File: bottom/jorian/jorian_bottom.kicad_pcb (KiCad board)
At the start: 2 copper layers, 152.4 x 85.1 mm, 7 parts

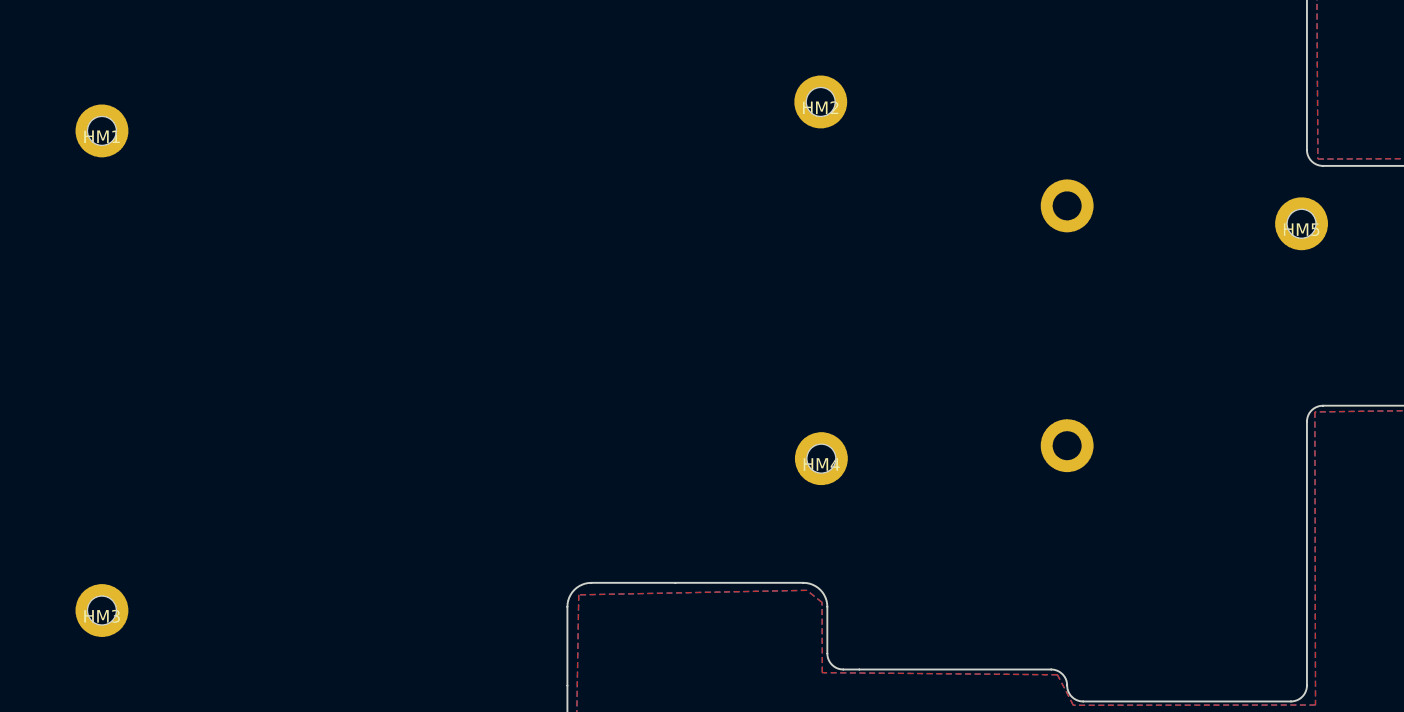
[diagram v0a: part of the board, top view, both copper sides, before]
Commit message: Updated case hole footprints
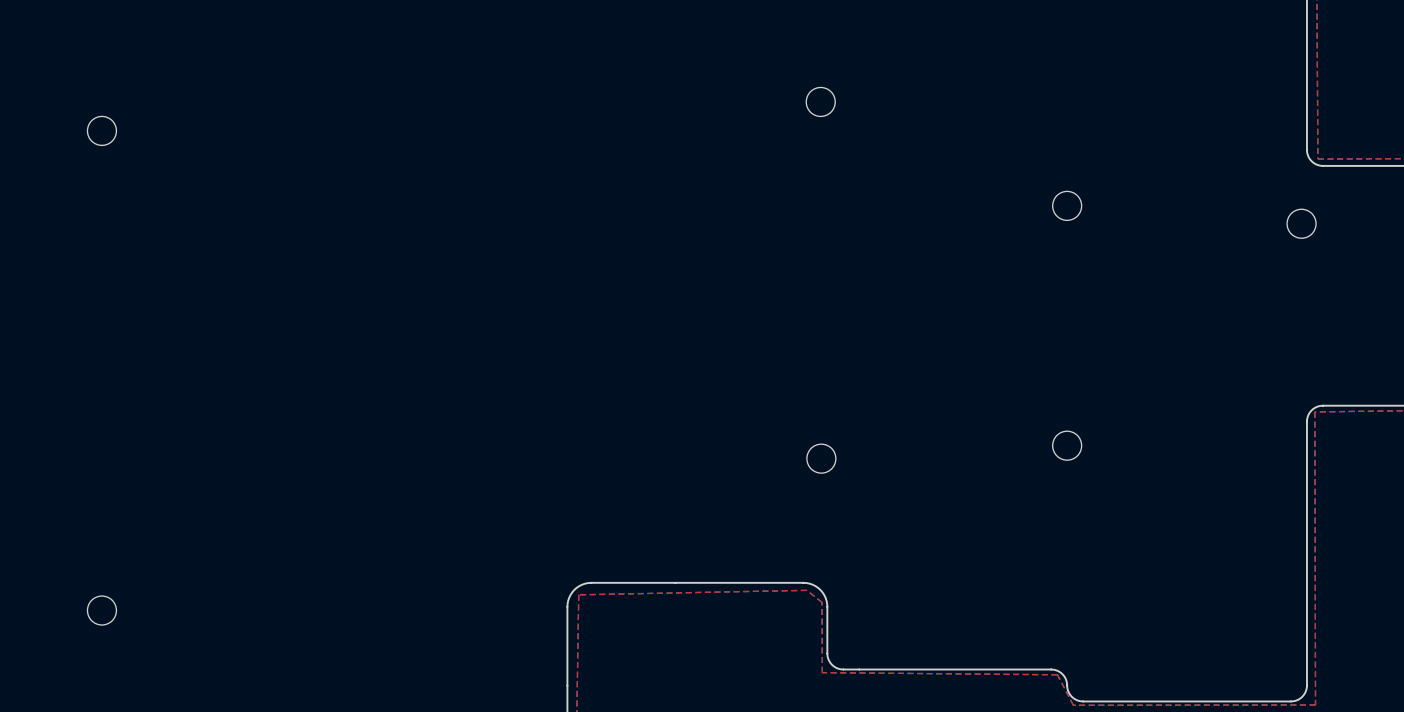
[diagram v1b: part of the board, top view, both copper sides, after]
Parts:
- HM1, HM2, HM3, HM4, HM5: footprint kbd:M2_Hole_TH_mod -> kbd:M2_Hole_Edge_Cut
- HM6, HM7: renamed from ?; value (none) -> CaseHole; footprint (none) -> kbd:M2_Hole_Edge_Cut
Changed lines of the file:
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@@
   (net 0 "")
   (net 1 "GND")
-  (footprint "" (layer "F.Cu")
+  (footprint "kbd:M2_Hole_Edge_Cut" (layer "F.Cu")
     (at 136.525 88.9)
-    (fp_text reference "" (at 0 0) (layer "F.SilkS")
-      (effects (font (size 1.27 1.27) (thickness 0.15)))
+    (fp_text reference "HM7" (at 0 1.9) (layer "Dwgs.User")
+      (effects (font (size 1 1) (thickness 0.15)))
     )
-    (fp_text value "" (at 0 0) (layer "F.SilkS")
-      (effects (font (size 1.27 1.27) (thickness 0.15)))
+    (fp_text value "CaseHole" (at 0 -1.8) (layer "F.Fab")
+      (effects (font (size 1 1) (thickness 0.15)))
     )
-    (pad "" thru_hole circle (at 0 0) (size 4.2 4.2) (drill 2.3) (layers *.Cu *.Mask))
+    (fp_circle (center 0 0) (end 1.15 0) (layer "Edge.Cuts") (width 0.1) (fill none))
   )
-  (footprint "kbd:M2_Hole_TH_mod" (layer "F.Cu")
+  (footprint "kbd:M2_Hole_Edge_Cut" (layer "F.Cu")
     (at 59.85 101.995)
     (property "Sheetfile" "jorian.kicad_sch")
     (property "Sheetname" "")
-    (fp_text reference "HM3" (at 0 0.5) (layer "F.SilkS")
+    (fp_text reference "HM3" (at 0 1.9) (layer "Dwgs.User")
       (effects (font (size 1 1) (thickness 0.15)))
     )
-    (fp_text value "CaseHole" (at 0 -0.5) (layer "F.Fab")
-      (effects (font (size 1 1) (thickness 0.15)))
-    )
-    (fp_text user "${REFERENCE}" (at 0.3 0) (layer "F.Fab")
+    (fp_text value "CaseHole" (at 0 -1.8) (layer "F.Fab")
       (effects (font (size 1 1) (thickness 0.15)))
     )
     (fp_circle (center 0 0) (end 1.15 0) (layer "Edge.Cuts") (width 0.1) (fill none))
-    (pad "" thru_hole circle (at 0 0) (size 4.2 4.2) (drill 2.3) (layers *.Cu *.Mask))
   )
-  (footprint "kbd:M2_Hole_TH_mod" (layer "F.Cu")
+  (footprint "kbd:M2_Hole_Edge_Cut" (layer "F.Cu")
     (at 155.145948 71.270959)
     (property "Sheetfile" "jorian.kicad_sch")
     (property "Sheetname" "")
-    (fp_text reference "HM5" (at 0 0.5) (layer "F.SilkS")
+    (fp_text reference "HM5" (at 0 1.9) (layer "Dwgs.User")
       (effects (font (size 1 1) (thickness 0.15)))
     )
-    (fp_text value "CaseHole" (at 0 -0.5) (layer "F.Fab")
-      (effects (font (size 1 1) (thickness 0.15)))
-    )
-    (fp_text user "${REFERENCE}" (at 0.3 0) (layer "F.Fab")
+    (fp_text value "CaseHole" (at 0 -1.8) (layer "F.Fab")
       (effects (font (size 1 1) (thickness 0.15)))
     )
     (fp_circle (center 0 0) (end 1.15 0) (layer "Edge.Cuts") (width 0.1) (fill none))
-    (pad "" thru_hole circle (at 0 0) (size 4.2 4.2) (drill 2.3) (layers *.Cu *.Mask))
   )
-  (footprint "kbd:M2_Hole_TH_mod" (layer "F.Cu")
+  (footprint "kbd:M2_Hole_Edge_Cut" (layer "F.Cu")
     (at 116.95 61.595)
     (property "Sheetfile" "jorian.kicad_sch")
     (property "Sheetname" "")
-    (fp_text reference "HM2" (at 0 0.5) (layer "F.SilkS")
+    (fp_text reference "HM2" (at 0 1.9) (layer "Dwgs.User")
       (effects (font (size 1 1) (thickness 0.15)))
     )
-    (fp_text value "CaseHole" (at 0 -0.5) (layer "F.Fab")
-      (effects (font (size 1 1) (thickness 0.15)))
-    )
-    (fp_text user "${REFERENCE}" (at 0.3 0) (layer "F.Fab")
+    (fp_text value "CaseHole" (at 0 -1.8) (layer "F.Fab")
       (effects (font (size 1 1) (thickness 0.15)))
     )
     (fp_circle (center 0 0) (end 1.15 0) (layer "Edge.Cuts") (width 0.1) (fill none))
-    (pad "" thru_hole circle (at 0 0) (size 4.2 4.2) (drill 2.3) (layers *.Cu *.Mask))
   )
-  (footprint "" (layer "F.Cu")
+  (footprint "kbd:M2_Hole_Edge_Cut" (layer "F.Cu")
     (at 136.525 69.85)
-    (fp_text reference "" (at 0 0) (layer "F.SilkS")
-      (effects (font (size 1.27 1.27) (thickness 0.15)))
+    (fp_text reference "HM6" (at 0 1.9) (layer "Dwgs.User")
+      (effects (font (size 1 1) (thickness 0.15)))
     )
-    (fp_text value "" (at 0 0) (layer "F.SilkS")
-      (effects (font (size 1.27 1.27) (thickness 0.15)))
+    (fp_text value "CaseHole" (at 0 -1.8) (layer "F.Fab")
+      (effects (font (size 1 1) (thickness 0.15)))
     )
-    (pad "" thru_hole circle (at 0 0) (size 4.2 4.2) (drill 2.3) (layers *.Cu *.Mask))
+    (fp_circle (center 0 0) (end 1.15 0) (layer "Edge.Cuts") (width 0.1) (fill none))
   )
-  (footprint "kbd:M2_Hole_TH_mod" (layer "F.Cu")
+  (footprint "kbd:M2_Hole_Edge_Cut" (layer "F.Cu")
     (at 117 89.93)
     (property "Sheetfile" "jorian.kicad_sch")
     (property "Sheetname" "")
-    (fp_text reference "HM4" (at 0 0.5) (layer "F.SilkS")
+    (fp_text reference "HM4" (at 0 1.9) (layer "Dwgs.User")
       (effects (font (size 1 1) (thickness 0.15)))
     )
-    (fp_text value "CaseHole" (at 0 -0.5) (layer "F.Fab")
-      (effects (font (size 1 1) (thickness 0.15)))
-    )
-    (fp_text user "${REFERENCE}" (at 0.3 0) (layer "F.Fab")
+    (fp_text value "CaseHole" (at 0 -1.8) (layer "F.Fab")
       (effects (font (size 1 1) (thickness 0.15)))
     )
     (fp_circle (center 0 0) (end 1.15 0) (layer "Edge.Cuts") (width 0.1) (fill none))
-    (pad "" thru_hole circle (at 0 0) (size 4.2 4.2) (drill 2.3) (layers *.Cu *.Mask))
   )
-  (footprint "kbd:M2_Hole_TH_mod" (layer "F.Cu")
+  (footprint "kbd:M2_Hole_Edge_Cut" (layer "F.Cu")
     (at 59.85 63.895)
     (property "Sheetfile" "jorian.kicad_sch")
     (property "Sheetname" "")
-    (fp_text reference "HM1" (at 0 0.5) (layer "F.SilkS")
+    (fp_text reference "HM1" (at 0 1.9) (layer "Dwgs.User")
       (effects (font (size 1 1) (thickness 0.15)))
     )
-    (fp_text value "CaseHole" (at 0 -0.5) (layer "F.Fab")
-      (effects (font (size 1 1) (thickness 0.15)))
-    )
-    (fp_text user "${REFERENCE}" (at 0.3 0) (layer "F.Fab")
+    (fp_text value "CaseHole" (at 0 -1.8) (layer "F.Fab")
       (effects (font (size 1 1) (thickness 0.15)))
     )
     (fp_circle (center 0 0) (end 1.15 0) (layer "Edge.Cuts") (width 0.1) (fill none))
-    (pad "" thru_hole circle (at 0 0) (size 4.2 4.2) (drill 2.3) (layers *.Cu *.Mask))
   )
   (gr_arc (start 97.155 38.735) (mid 98.053026 39.106974) (end 98.425 40.005) (layer "Edge.Cuts") (width 0.15))
